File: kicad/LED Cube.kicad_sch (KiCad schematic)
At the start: 29 parts, among them Q1 2N3904, Q2 2N3904, Q3 2N3904, Q4 2N3904, U2 74HC595, U3 74HC595

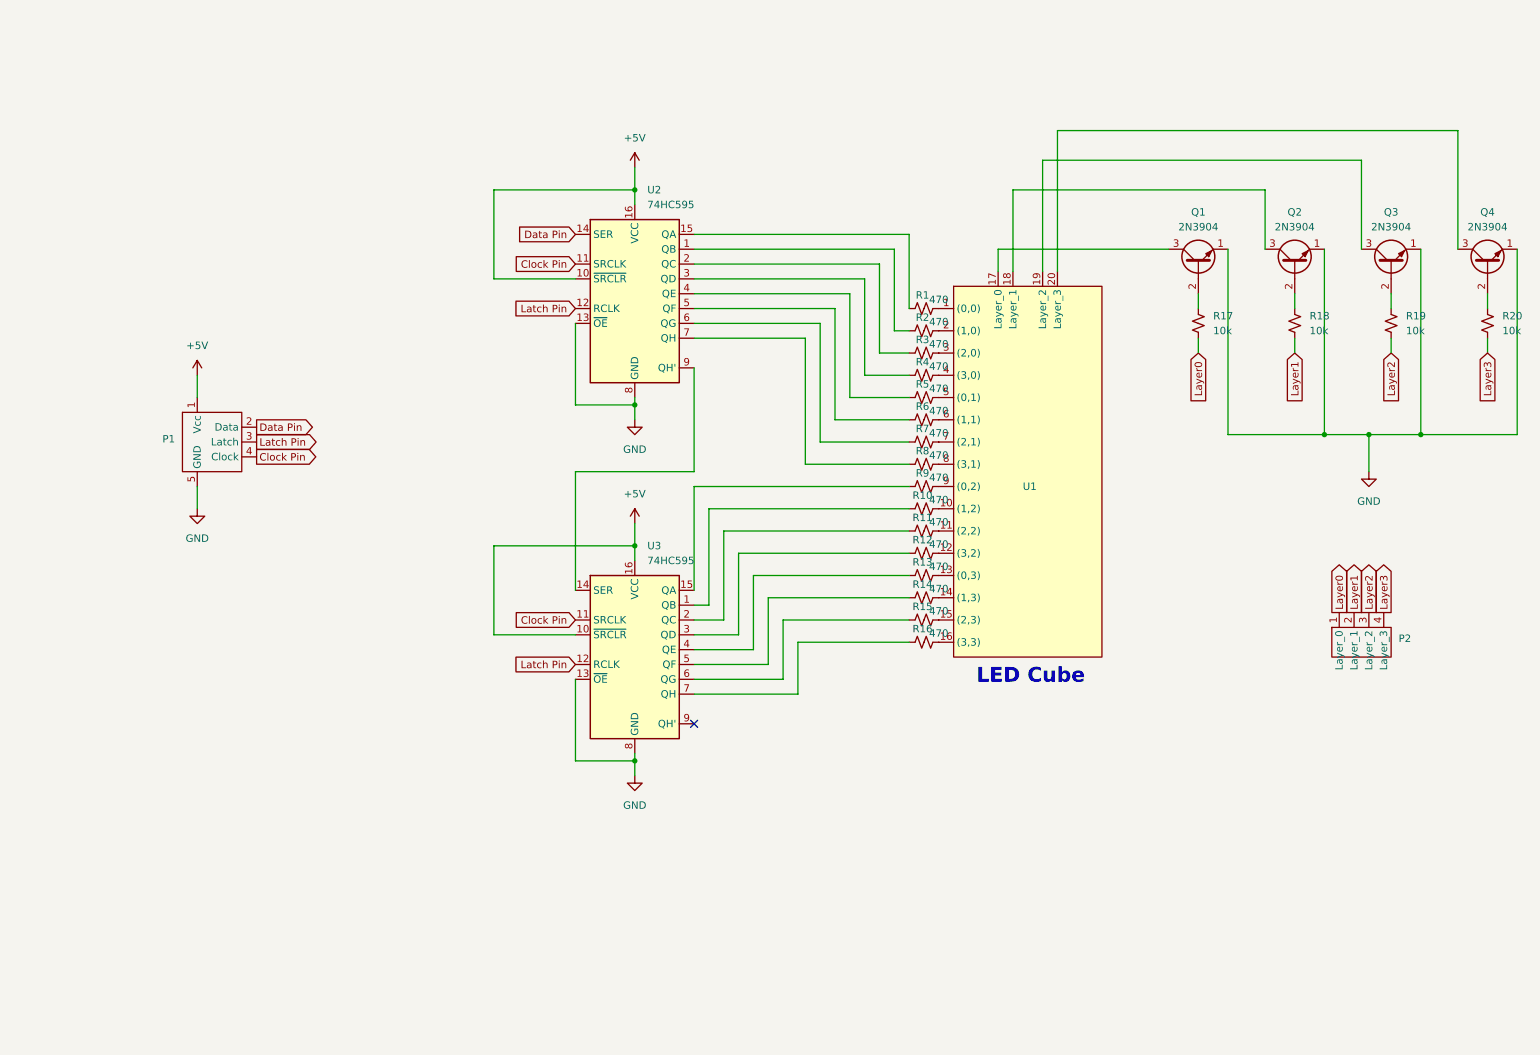
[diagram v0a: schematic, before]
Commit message: added schematics for top and side view
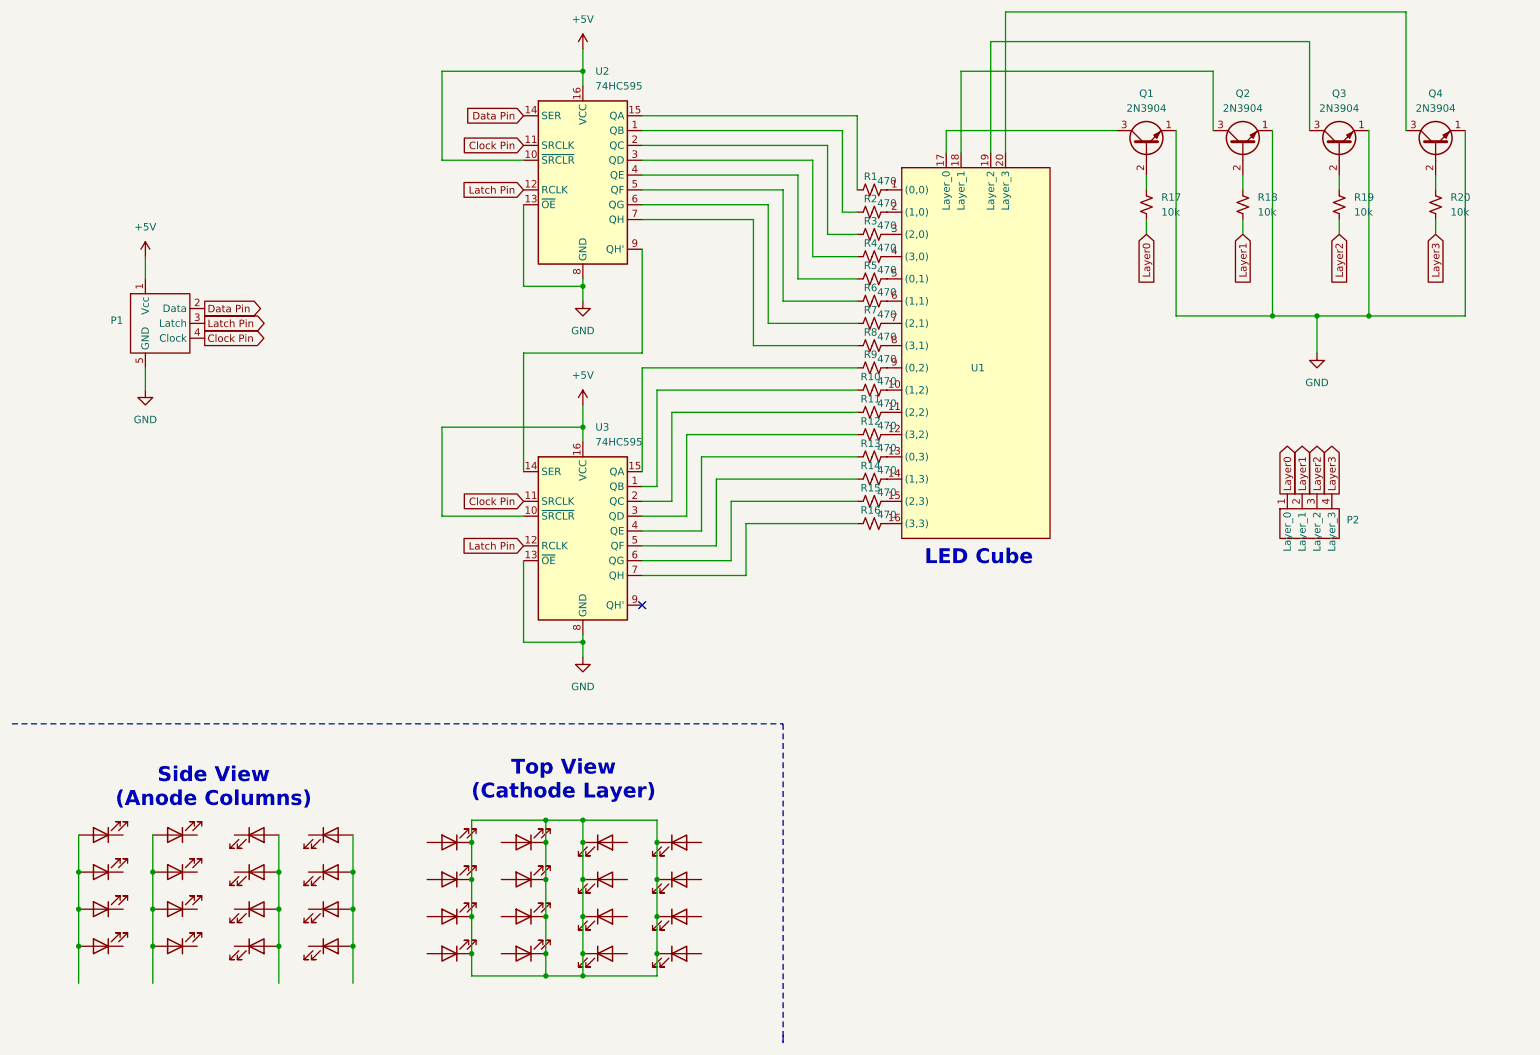
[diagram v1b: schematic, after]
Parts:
- added D1, D10, D11, D12, D13, D14, D15, D16, D17, D18, D19, D2, D20, D21, D22, D23, D24, D25, D26, D27, D28, D29, D3, D30, D31, D32, D4, D5, D6, D7, D8, D9: LED, symbol Device:LED
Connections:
- new net: D13.2 (A), D14.2 (A), D15.2 (A), D16.2 (A)
- new net: D17.1 (K), D18.1 (K), D19.1 (K), D20.1 (K), D21.1 (K), D22.1 (K), D23.1 (K), D24.1 (K), D25.1 (K), D26.1 (K), D27.1 (K), D28.1 (K), D29.1 (K), D30.1 (K), D31.1 (K), D32.1 (K)
- new net: D1.2 (A), D2.2 (A), D3.2 (A), D4.2 (A)
- new net: D10.2 (A), D11.2 (A), D12.2 (A), D9.2 (A)
- new net: D5.2 (A), D6.2 (A), D7.2 (A), D8.2 (A)
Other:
- note added: "Side View (Anode Columns)"
- note added: "Top View (Cathode Layer)"
- moved on the sheet: P1, P2, Q1, Q2, Q3, Q4, R1, R10, R11, R12, R13, R14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
